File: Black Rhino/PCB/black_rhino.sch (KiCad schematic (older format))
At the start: 178 parts, among them SW1 SW_Push, U1 ATmega32U4-AU, Y1 16MHz

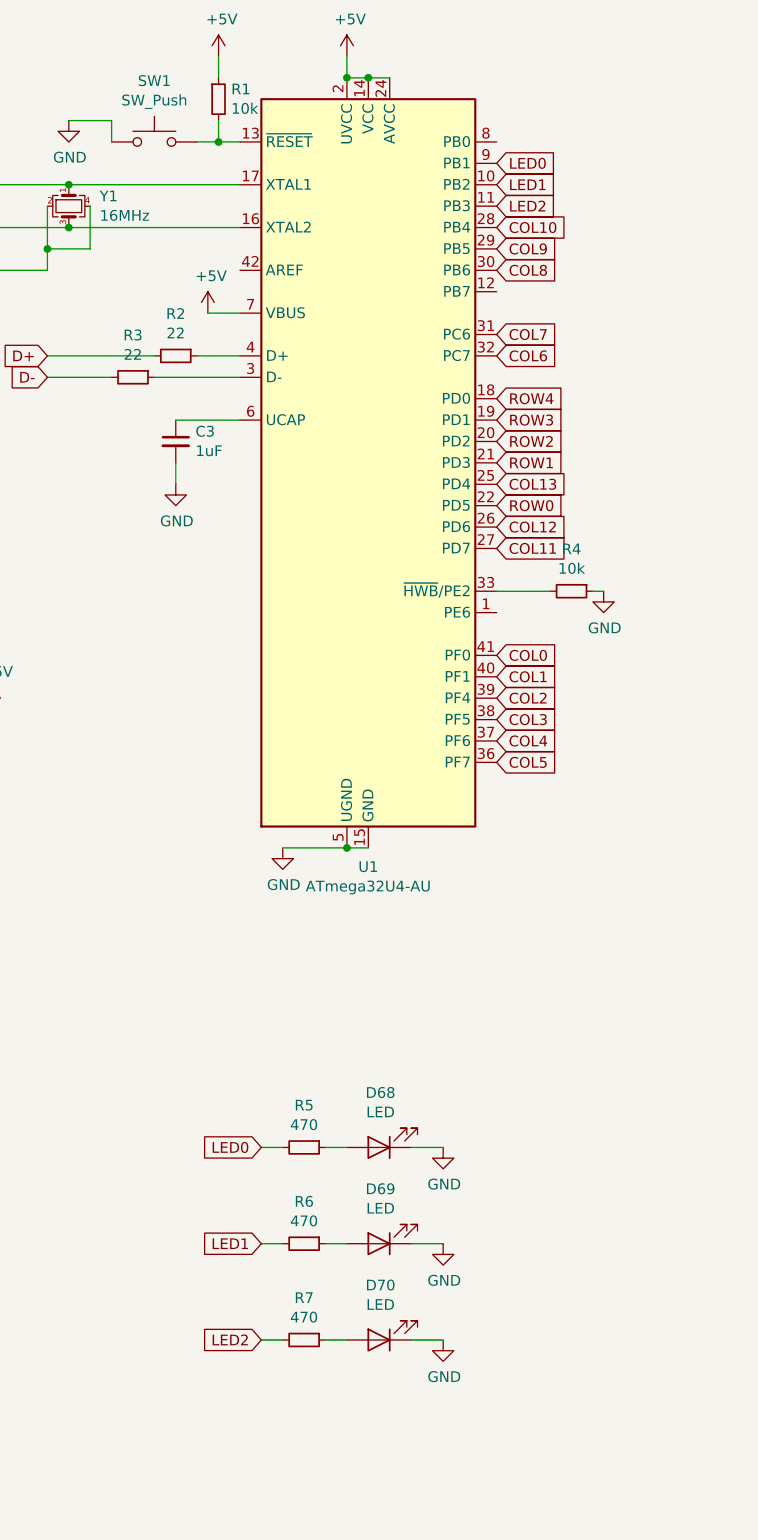
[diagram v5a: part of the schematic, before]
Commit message: Fix Black Rhino-PCB
I only needed 1 Indicator-LED and added 3 in commit:
67b9c5aa973747f4bc26af49aa7426545263447c
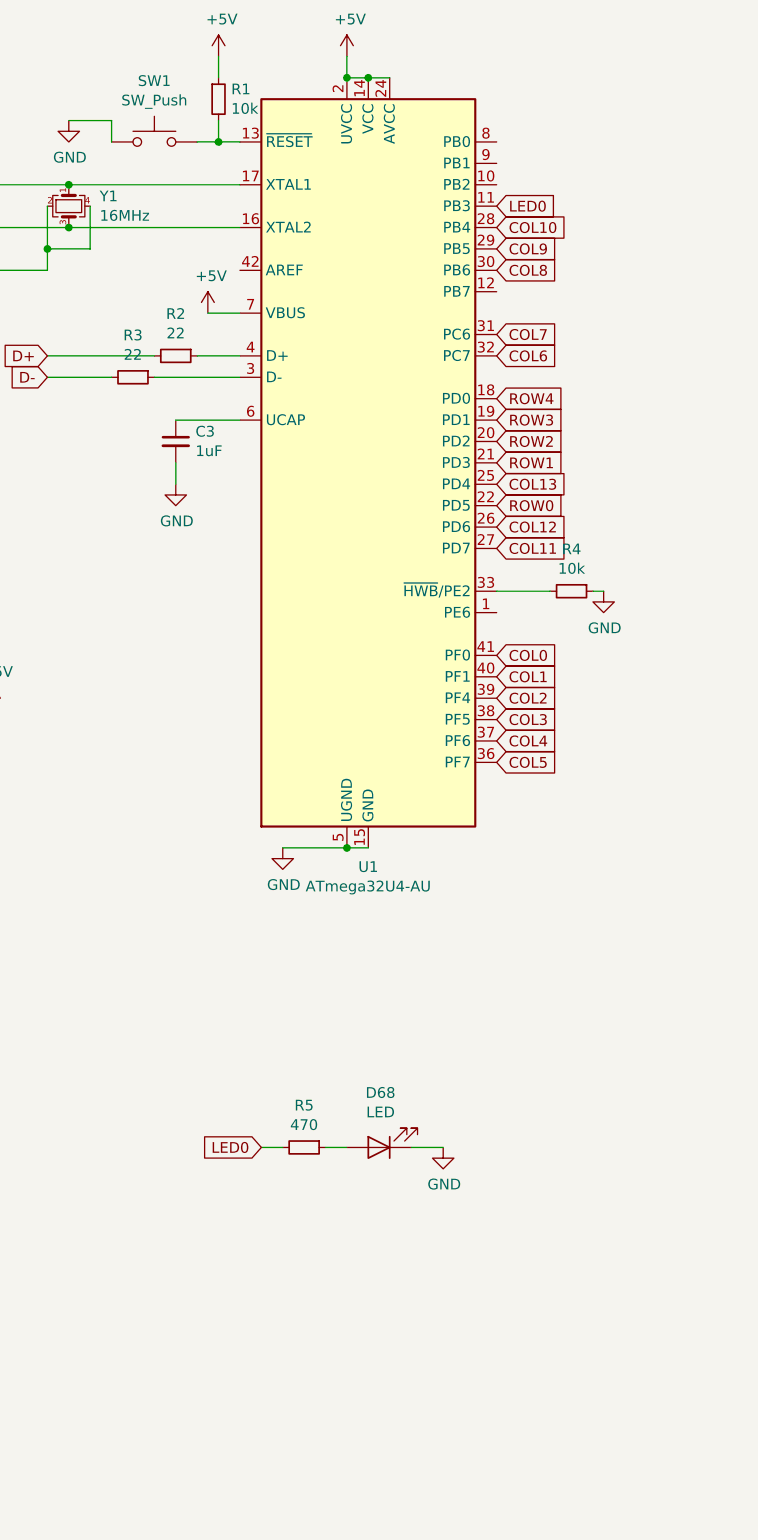
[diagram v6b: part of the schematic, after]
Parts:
- removed D69, D70: LED, LED_SMD:LED_0805_2012Metric, symbol Device:LED
- removed R6, R7: 470, Resistor_SMD:R_0805_2012Metric, symbol Device:R_Small
- MX28, MX60, MX61: footprint MX_Alps_Hybrid:MX-1U -> MX_Alps_Hybrid:MX-2U
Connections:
- net LED2 is gone; now on net LED0: U1.11 (PB3)
- net LED0: no longer U1.9 (PB1)
- net LED1: no longer names the net of U1.10 (PB2)
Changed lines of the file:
@@
 F 0 "MX61" H 11633 4573 60  0000 C CNN
 F 1 "MX-NoLED" H 11633 4499 20  0000 C CNN
-F 2 "MX_Alps_Hybrid:MX-1U" H 10975 4325 60  0001 C CNN
+F 2 "MX_Alps_Hybrid:MX-2U" H 10975 4325 60  0001 C CNN
 F 3 "" H 10975 4325 60  0001 C CNN
 	1    11600 4350
@@
 F 0 "MX60" H 11133 4573 60  0000 C CNN
 F 1 "MX-NoLED" H 11133 4499 20  0000 C CNN
-F 2 "MX_Alps_Hybrid:MX-1U" H 10475 4325 60  0001 C CNN
+F 2 "MX_Alps_Hybrid:MX-2U" H 10475 4325 60  0001 C CNN
 F 3 "" H 10475 4325 60  0001 C CNN
 	1    11100 4350
@@
 F 0 "MX28" H 15133 2623 60  0000 C CNN
 F 1 "MX-NoLED" H 15133 2549 20  0000 C CNN
-F 2 "MX_Alps_Hybrid:MX-1U" H 14475 2375 60  0001 C CNN
+F 2 "MX_Alps_Hybrid:MX-2U" H 14475 2375 60  0001 C CNN
 F 3 "" H 14475 2375 60  0001 C CNN
 	1    15100 2400
@@
 	1    0    0    -1
 $EndComp
-$Comp
-L Device:LED D69
-U 1 1 5F2AC4F2
-P 4200 6650
-F 0 "D69" H 4193 6395 50  0000 C CNN
-F 1 "LED" H 4193 6486 50  0000 C CNN
-F 2 "LED_SMD:LED_0805_2012Metric" H 4200 6650 50  0001 C CNN
-F 3 "~" H 4200 6650 50  0001 C CNN
-	1    4200 6650
-	-1   0    0    1
-$EndComp
-$Comp
-L Device:R_Small R6
-U 1 1 5F2AC4F8
-P 3850 6650
-F 0 "R6" V 3654 6650 50  0000 C CNN
-F 1 "470" V 3745 6650 50  0000 C CNN
-F 2 "Resistor_SMD:R_0805_2012Metric" H 3850 6650 50  0001 C CNN
-F 3 "~" H 3850 6650 50  0001 C CNN
-	1    3850 6650
-	0    1    1    0
-$EndComp
-$Comp
-L power:GND #PWR0115
-U 1 1 5F2AC4FE
-P 4500 6650
-F 0 "#PWR0115" H 4500 6400 50  0001 C CNN
-F 1 "GND" H 4505 6477 50  0000 C CNN
-F 2 "" H 4500 6650 50  0001 C CNN
-F 3 "" H 4500 6650 50  0001 C CNN
-	1    4500 6650
-	1    0    0    -1
-$EndComp
-$Comp
-L Device:LED D70
-U 1 1 5F2BE790
-P 4200 7100
-F 0 "D70" H 4193 6845 50  0000 C CNN
-F 1 "LED" H 4193 6936 50  0000 C CNN
-F 2 "LED_SMD:LED_0805_2012Metric" H 4200 7100 50  0001 C CNN
-F 3 "~" H 4200 7100 50  0001 C CNN
-	1    4200 7100
-	-1   0    0    1
-$EndComp
-$Comp
-L Device:R_Small R7
-U 1 1 5F2BE796
-P 3850 7100
-F 0 "R7" V 3654 7100 50  0000 C CNN
-F 1 "470" V 3745 7100 50  0000 C CNN
-F 2 "Resistor_SMD:R_0805_2012Metric" H 3850 7100 50  0001 C CNN
-F 3 "~" H 3850 7100 50  0001 C CNN
-	1    3850 7100
-	0    1    1    0
-$EndComp
-$Comp
-L power:GND #PWR0116
-U 1 1 5F2BE79C
-P 4500 7100
-F 0 "#PWR0116" H 4500 6850 50  0001 C CNN
-F 1 "GND" H 4505 6927 50  0000 C CNN
-F 2 "" H 4500 7100 50  0001 C CNN
-F 3 "" H 4500 7100 50  0001 C CNN
-	1    4500 7100
-	1    0    0    -1
-$EndComp
-Text GLabel 4750 1600 2    50   Input ~ 0
+Text GLabel 4750 1800 2    50   Input ~ 0
 LED0
-Text GLabel 4750 1700 2    50   Input ~ 0
-LED1
-Text GLabel 4750 1800 2    50   Input ~ 0
-LED2
 Text GLabel 3650 6200 0    50   Input ~ 0
 LED0
-Text GLabel 3650 6650 0    50   Input ~ 0
-LED1
-Text GLabel 3650 7100 0    50   Input ~ 0
-LED2
 Wire Wire Line
 	3650 6200 3750 6200
@@
 	3950 6200 4050 6200
 Wire Wire Line
-	3650 6650 3750 6650
-Wire Wire Line
-	3950 6650 4050 6650
-Wire Wire Line
-	3650 7100 3750 7100
-Wire Wire Line
-	3950 7100 4050 7100
-Wire Wire Line
 	4350 6200 4500 6200
-Wire Wire Line
-	4350 6650 4500 6650
-Wire Wire Line
-	4350 7100 4500 7100
 $Comp
 L Device:R_Small R5

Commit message: Improve Black Rhino-PCB
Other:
- moved on the sheet: C1, C2, C4, C5, C6, C7, D68, F1, R1, R2, R3, R4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
